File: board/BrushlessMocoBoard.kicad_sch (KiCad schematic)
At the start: 0 parts

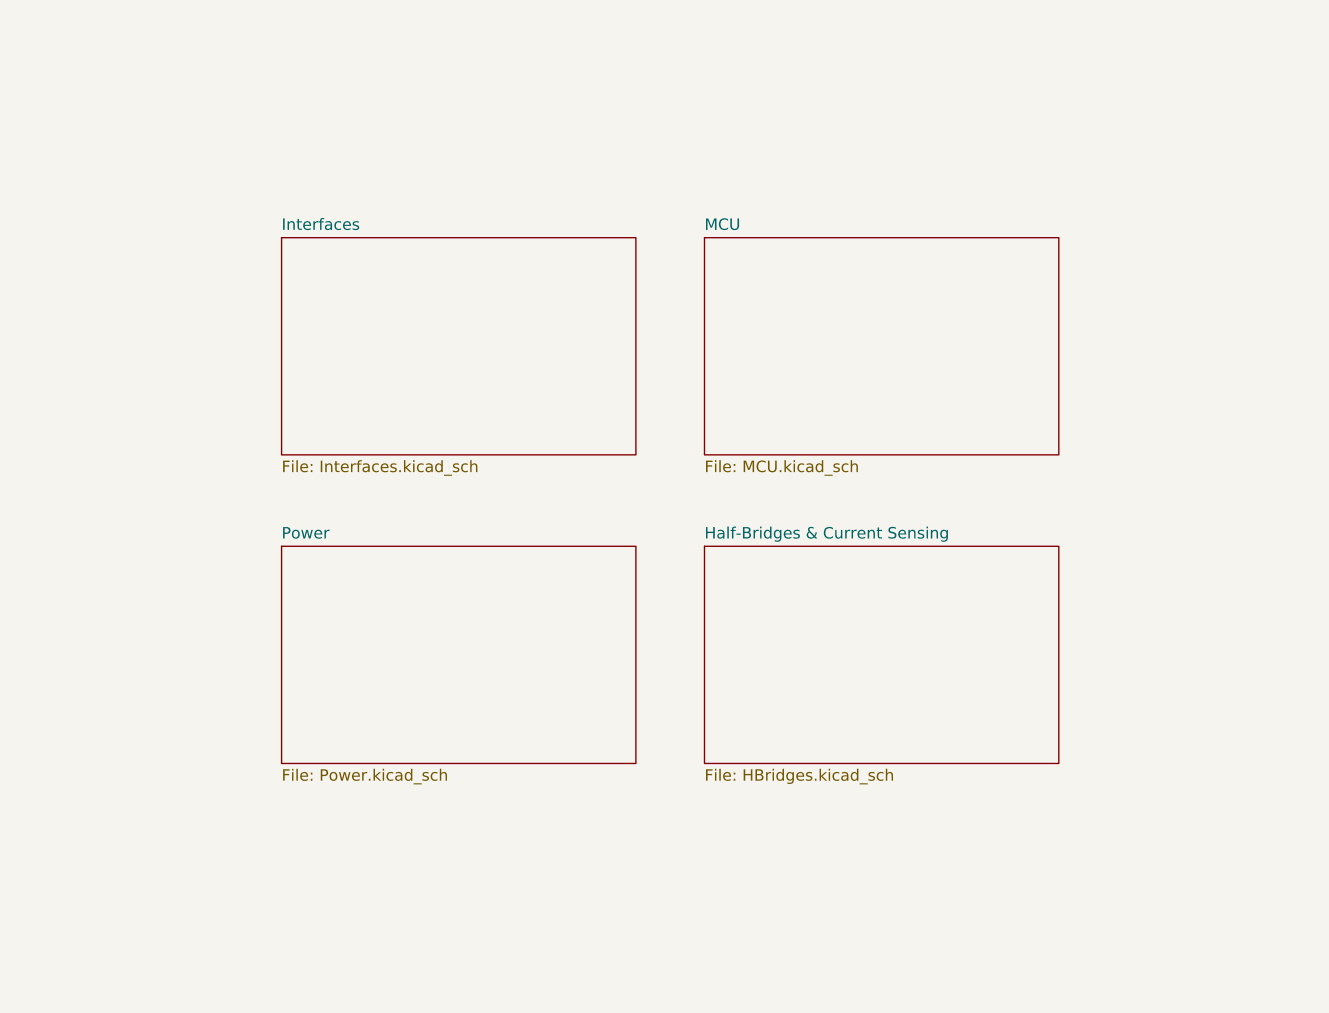
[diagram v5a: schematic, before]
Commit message: Fixed many issues brought up in the schematic review.
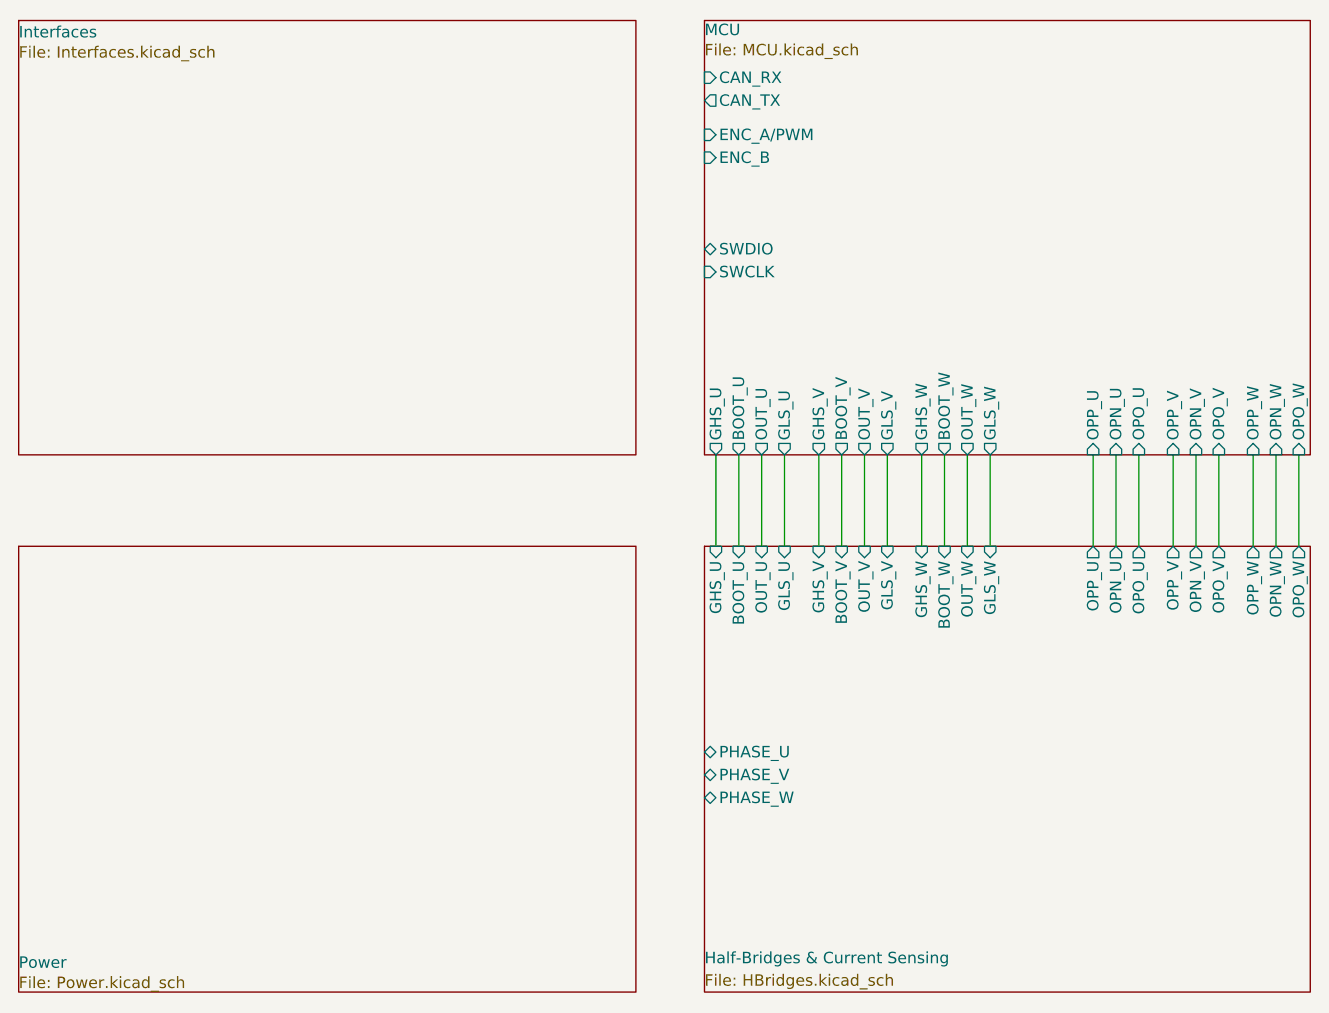
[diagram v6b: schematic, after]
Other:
- sheet Half-Bridges & Current Sensing ports: added BOOT_U, BOOT_V, BOOT_W, GHS_U, GHS_V, GHS_W, GLS_U, GLS_V, GLS_W, OPN_U, OPN_V, OPN_W, OPO_U, OPO_V, OPO_W, OPP_U, OPP_V, OPP_W, OUT_U, OUT_V, OUT_W, PHASE_U, PHASE_V, PHASE_W; removed none
- sheet MCU ports: added BOOT_U, BOOT_V, BOOT_W, CAN_RX, CAN_TX, ENC_A/PWM, ENC_B, GHS_U, GHS_V, GHS_W, GLS_U, GLS_V, GLS_W, OPN_U, OPN_V, OPN_W, OPO_U, OPO_V, OPO_W, OPP_U, OPP_V, OPP_W, OUT_U, OUT_V, OUT_W, SWCLK, SWDIO; removed none

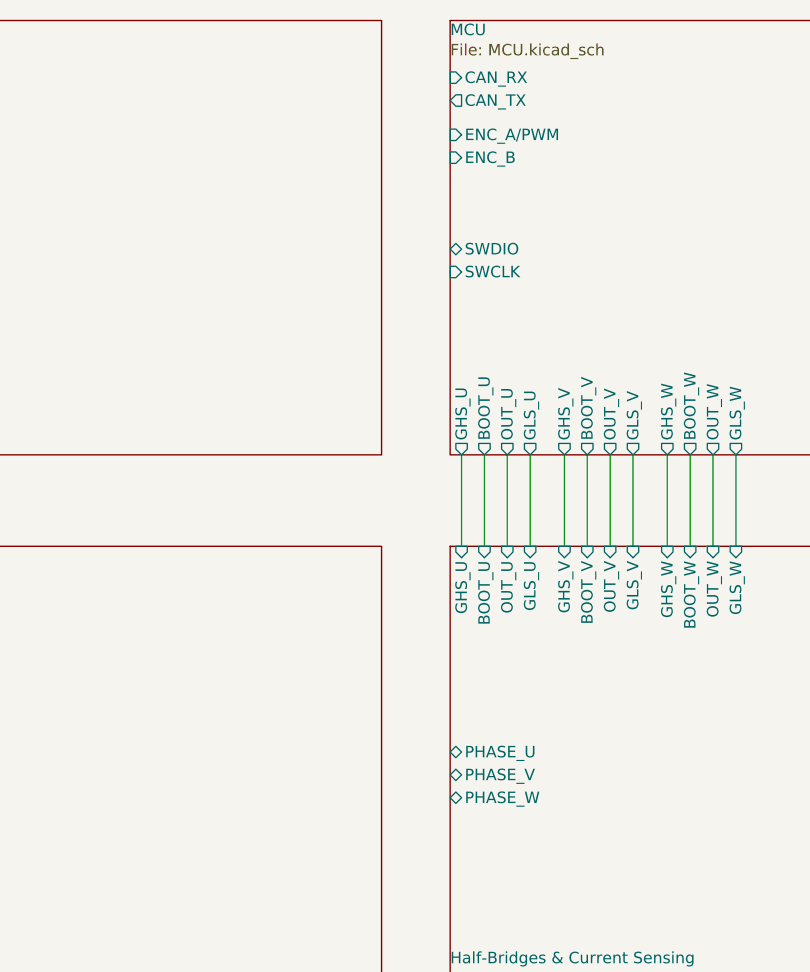
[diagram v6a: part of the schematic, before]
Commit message: Fixed everything mentioned in schematic review, should be ready for second review/layout.
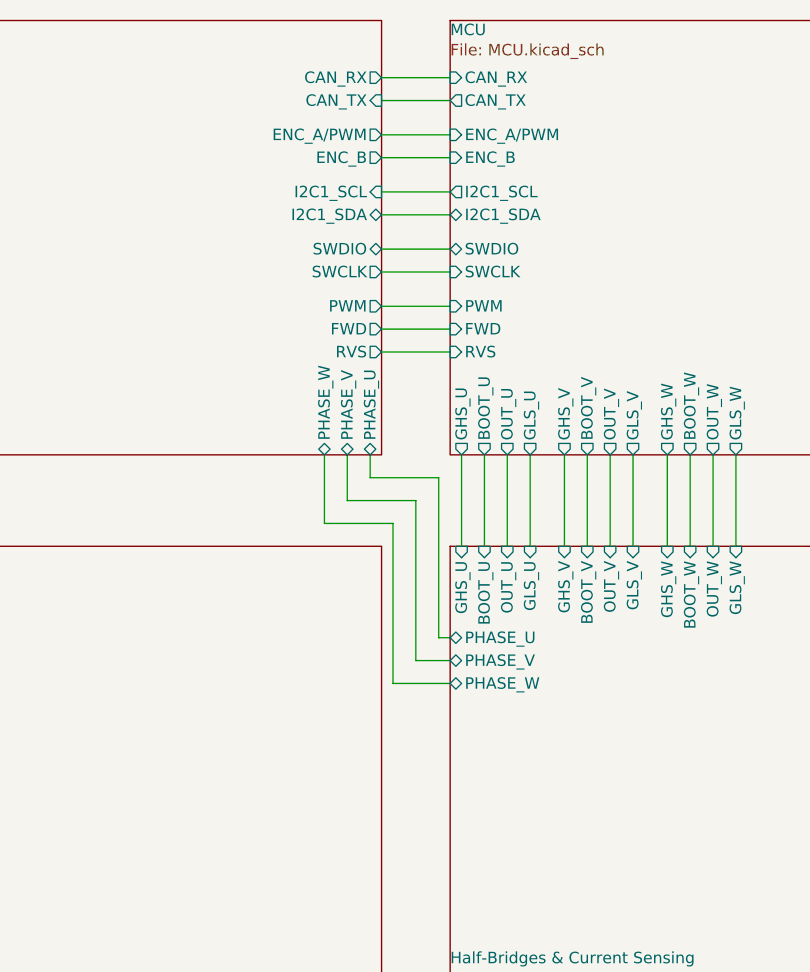
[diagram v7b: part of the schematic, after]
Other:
- sheet Interfaces ports: added CAN_RX, CAN_TX, ENC_A/PWM, ENC_B, FWD, I2C1_SCL, I2C1_SDA, PHASE_U, PHASE_V, PHASE_W, PWM, RVS, SWCLK, SWDIO; removed none
- sheet MCU ports: added FWD, I2C1_SCL, I2C1_SDA, PWM, RVS; removed none

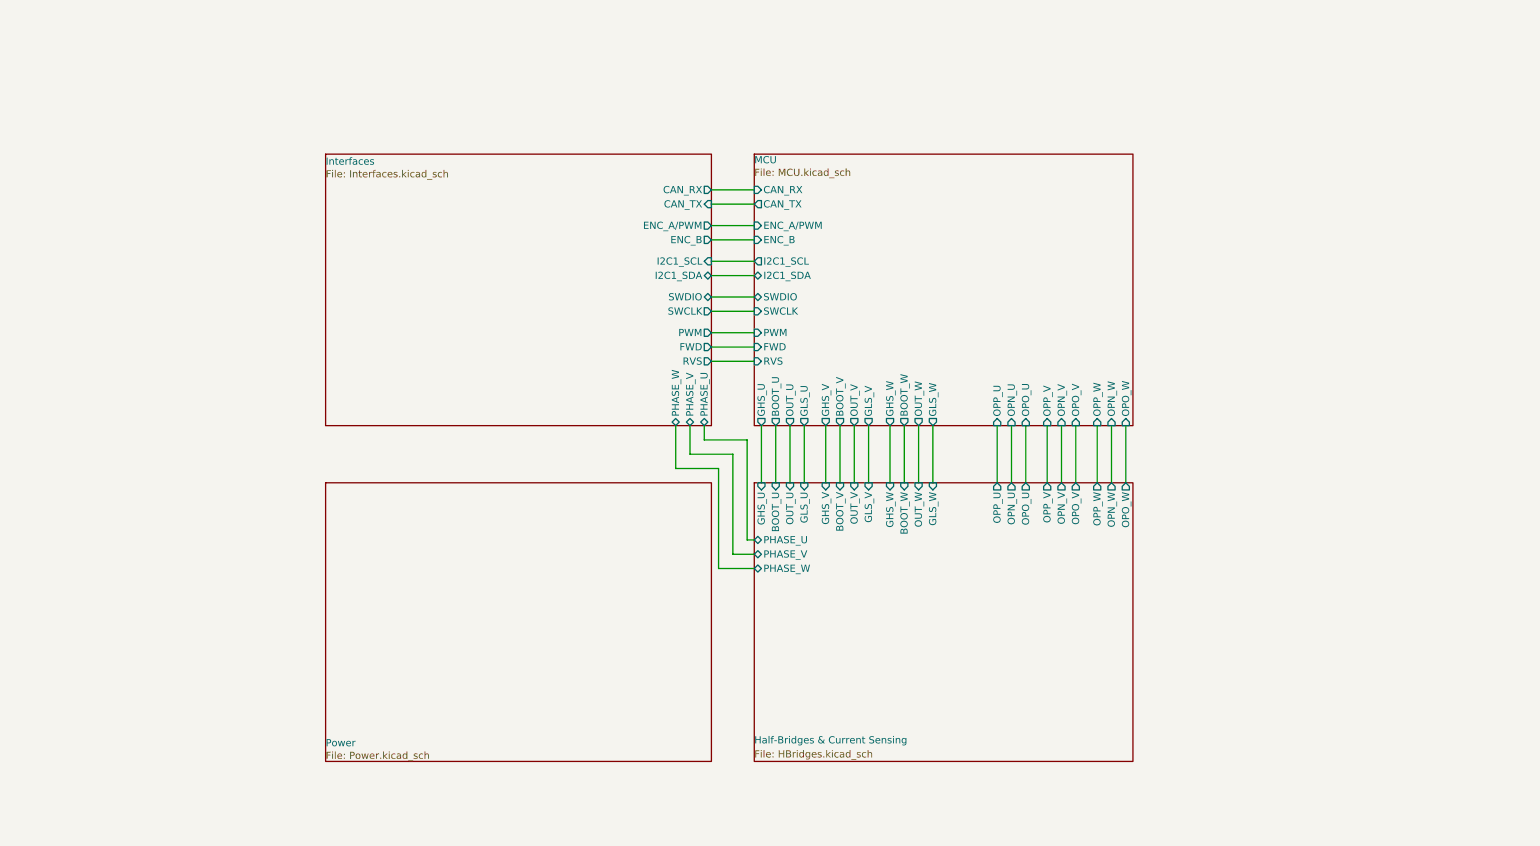
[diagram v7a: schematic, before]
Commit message: Rearranged components on the layout, added a switch, and connected hierarchical labels in the schematic.
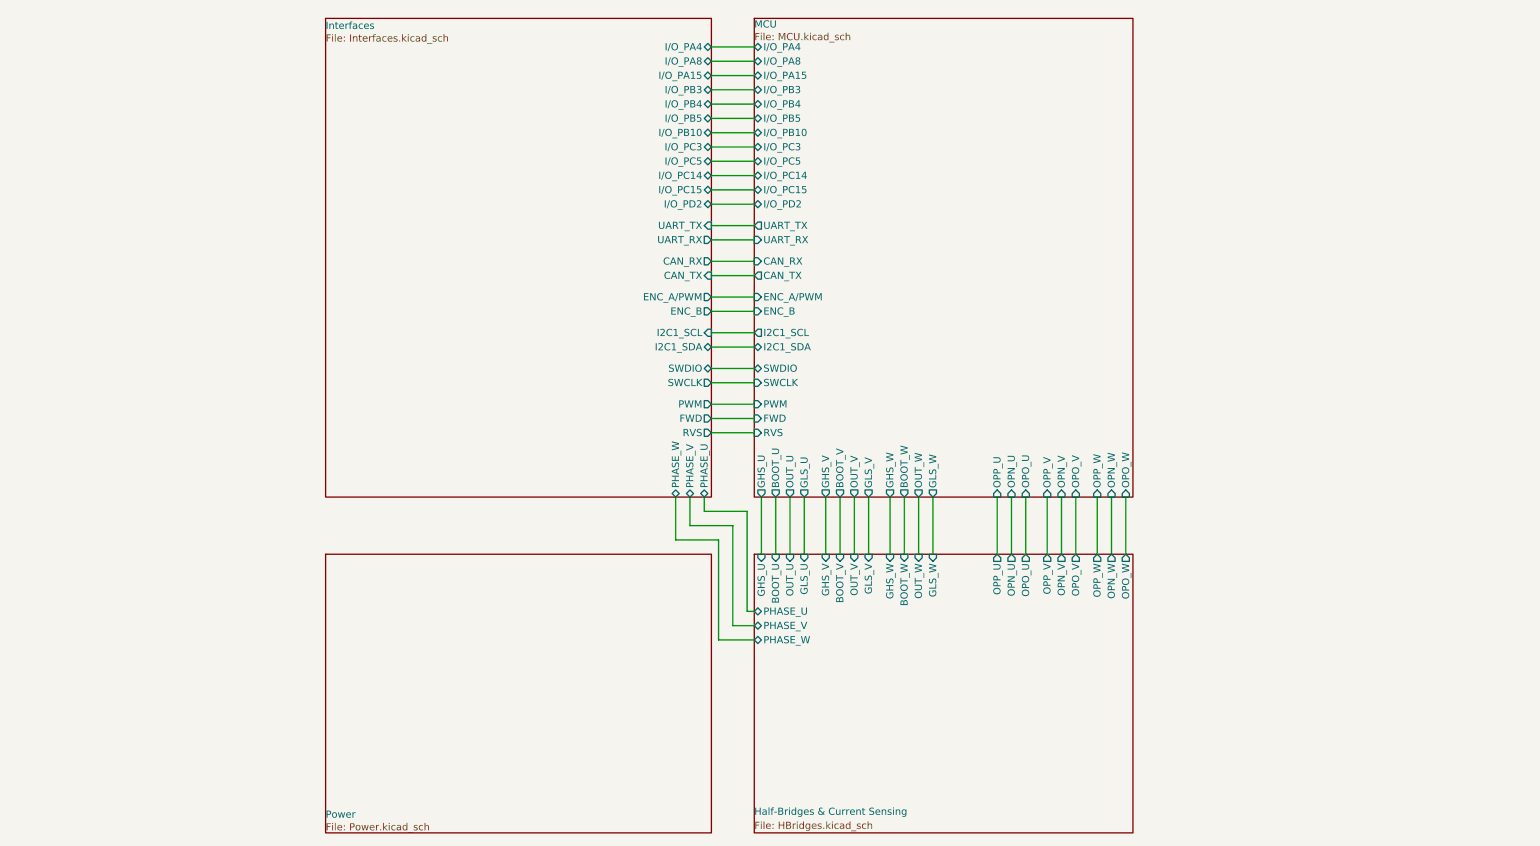
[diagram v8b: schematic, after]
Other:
- sheet Interfaces ports: added I/O_PA15, I/O_PA4, I/O_PA8, I/O_PB10, I/O_PB3, I/O_PB4, I/O_PB5, I/O_PC14, I/O_PC15, I/O_PC3, I/O_PC5, I/O_PD2, UART_RX, UART_TX; removed none
- sheet MCU ports: added I/O_PA15, I/O_PA4, I/O_PA8, I/O_PB10, I/O_PB3, I/O_PB4, I/O_PB5, I/O_PC14, I/O_PC15, I/O_PC3, I/O_PC5, I/O_PD2, UART_RX, UART_TX; removed none
